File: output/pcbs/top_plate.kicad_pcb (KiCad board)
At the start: 2 copper layers, 93.4 x 87.1 mm, 0 parts

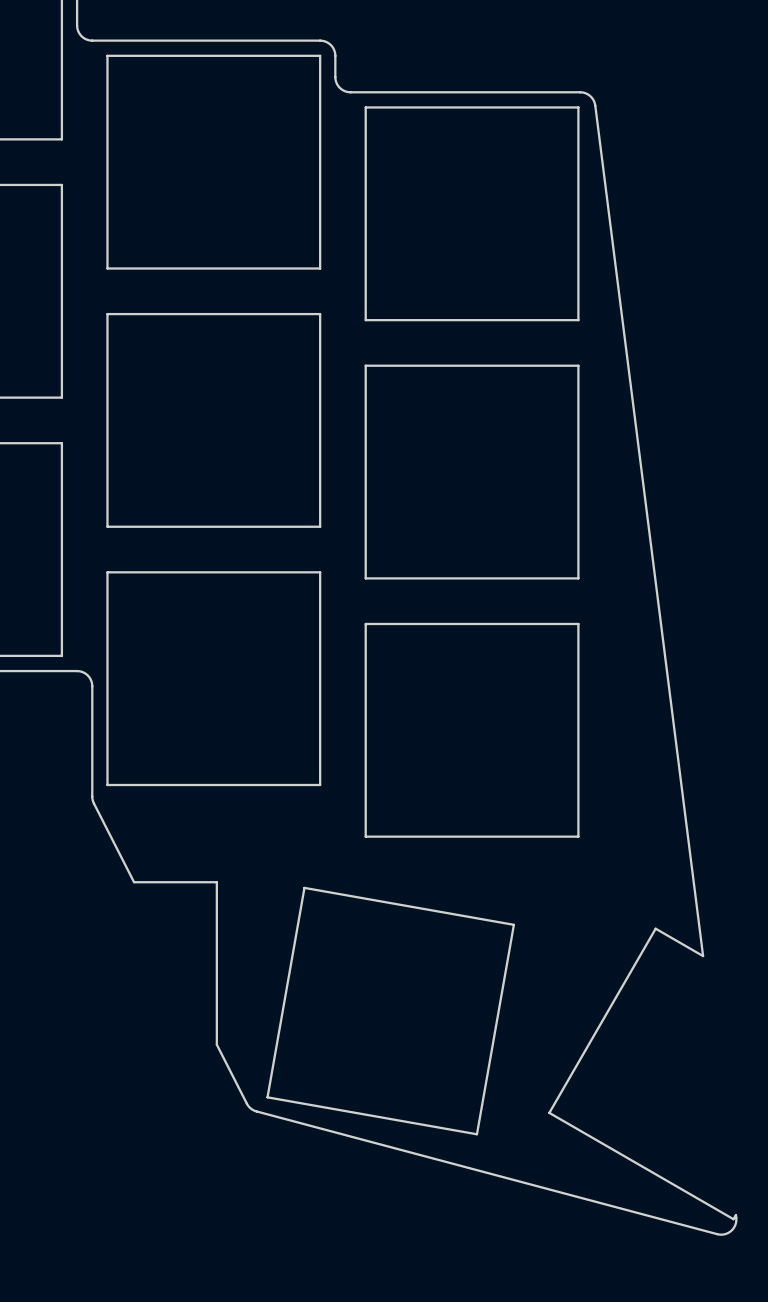
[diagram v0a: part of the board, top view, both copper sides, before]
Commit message: Close the design gaps: coin cell, per-key LEDs, ZMK dongle, JLC files, case
- Reversible footprints (2-pin SMD, SOT-23, slide switch, CR2032 holder,
  M2 holes) that mirror their B-side copper, so one PCB assembles as the
  left half on top and the right half on the bottom.
- Coin cell power path (CR2032 -> switch -> B5819W -> XIAO BAT+), per-key
  0603 LEDs with one PWM-dimmed low-side MOSFET.
- Routed board via Freerouting plus a finisher for nets it misreads, GND
  pours, DRC with no unconnected items, gerbers, BOM and CPL for both sides.
- ZMK v0.3 config: dongle central, two peripheral halves, backlight off by
  default at 10% with idle auto-off; GitHub Actions build.
- OpenSCAD uniboard case generated from the board outline.
- Old hand-routed LiPo board moved to archive/v1-lipo.

Co-Authored-By: Claude Opus 5.5 (1M context) <noreply@anthropic.com>
Claude-Session: https://claude.ai/code/session_01FPyenVXHBDq22rK9XranC3
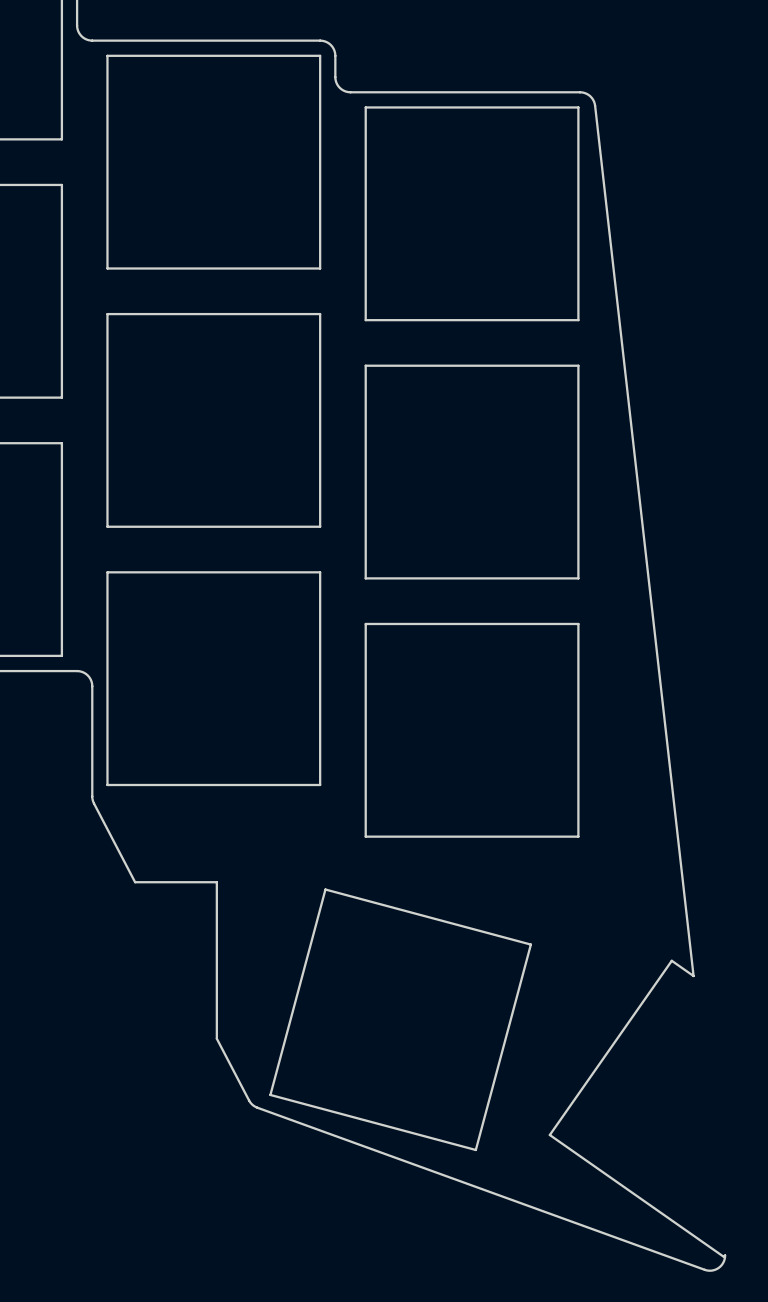
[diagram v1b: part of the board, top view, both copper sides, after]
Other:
- board size 93.4 x 87.1 mm -> 92.7 x 89.5 mm
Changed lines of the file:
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@@
   (page A3)
   (title_block
-    (title "top_plate")
-    (rev "v1.0.0")
-    (company "Unknown")
+    (title top_plate)
+    (rev v1.0.0)
+    (company Unknown)
   )
   (general
@@
       (outputdirectory ""))
   )
-  (net 0 "")
+            (net 0 "")
   (net_class Default "This is the default net class."
     (clearance 0.2)
@@
     (add_net "")
   )
-  (gr_line (start -8 7) (end -8 -41) (angle 90) (layer Edge.Cuts) (width 0.15))
+            (gr_line (start -8 7) (end -8 -41) (angle 90) (layer Edge.Cuts) (width 0.15))
 (gr_line (start -7 -42) (end 8 -42) (angle 90) (layer Edge.Cuts) (width 0.15))
 (gr_line (start 9 -43) (end 9 -54.6) (angle 90) (layer Edge.Cuts) (width 0.15))
@@
 (gr_line (start 43 -53.9) (end 58 -53.9) (angle 90) (layer Edge.Cuts) (width 0.15))
 (gr_line (start 59 -52.9) (end 59 -51.5) (angle 90) (layer Edge.Cuts) (width 0.15))
-(gr_line (start 60 -50.5) (end 75.11877832803583 -50.5) (angle 90) (layer Edge.Cuts) (width 0.15))
-(gr_line (start 76.11083692803584 -49.62577650000003) (end 83.2091607869865 6.362075546015262) (angle 90) (layer Edge.Cuts) (width 0.15))
-(gr_line (start 85.37063644510643 23.41066078283643) (end 85.39157132574321 23.575784130683587) (angle 90) (layer Edge.Cuts) (width 0.15))
-(gr_line (start 84.14207952574318 24.667856730683518) (end 53.808555992537784 16.586633122420103) (angle 90) (layer Edge.Cuts) (width 0.15))
-(gr_line (start 53.17493859253778 16.07424092242009) (end 51.2 12.197274108756417) (angle 90) (layer Edge.Cuts) (width 0.15))
-(gr_line (start 45.750776292981996 1.5) (end 43.1089494 -3.6861233712457846) (angle 90) (layer Edge.Cuts) (width 0.15))
-(gr_line (start 43 -4.140027271245785) (end 43 -11.399999999999999) (angle 90) (layer Edge.Cuts) (width 0.15))
+(gr_line (start 60 -50.5) (end 75.10676247796003 -50.5) (angle 90) (layer Edge.Cuts) (width 0.15))
+(gr_line (start 76.10042267796003 -49.61242549999997) (end 82.58220076816252 7.676038265248053) (angle 90) (layer Edge.Cuts) (width 0.15))
+(gr_line (start 83.31672830212476 27.014027452483596) (end 53.86711680697825 16.343062284377336) (angle 90) (layer Edge.Cuts) (width 0.15))
+(gr_line (start 53.32136560697827 15.865756084377338) (end 51.2 11.80327087166765) (angle 90) (layer Edge.Cuts) (width 0.15))
+(gr_line (start 45.81979470149059 1.5) (end 43.113577 -3.6824962931961807) (angle 90) (layer Edge.Cuts) (width 0.15))
+(gr_line (start 43 -4.145372393196169) (end 43 -11.399999999999999) (angle 90) (layer Edge.Cuts) (width 0.15))
 (gr_line (start 42 -12.399999999999999) (end 26 -12.399999999999999) (angle 90) (layer Edge.Cuts) (width 0.15))
 (gr_line (start 25 -11.399999999999999) (end 25 -6.6) (angle 90) (layer Edge.Cuts) (width 0.15))
@@
 (gr_arc (start 58 -52.9) (end 59 -52.9) (angle -90) (layer Edge.Cuts) (width 0.15))
 (gr_arc (start 60 -51.5) (end 59 -51.5) (angle -90) (layer Edge.Cuts) (width 0.15))
-(gr_arc (start 75.11877832803583 -49.5) (end 76.11083692803584 -49.6257765) (angle -82.77440010116284) (layer Edge.Cuts) (width 0.15))
-(gr_arc (start 84.39951272574318 23.701560630683502) (end 84.14207952574318 24.667856730683503) (angle -112.14341151228206) (layer Edge.Cuts) (width 0.15))
-(gr_arc (start 54.065989192537785 15.6203370224201) (end 53.174938592537785 16.0742409224201) (angle -48.08775587110787) (layer Edge.Cuts) (width 0.15))
-(gr_arc (start 44 -4.140027271245785) (end 43 -4.140027271245785) (angle -26.99443251544085) (layer Edge.Cuts) (width 0.15))
+(gr_arc (start 75.10676247796003 -49.5) (end 76.10042267796003 -49.6124255) (angle -83.5448462900765) (layer Edge.Cuts) (width 0.15))
+(gr_arc (start 83.65740010212473 26.073845152483727) (end 83.31672830212473 27.014027452483727) (angle -110.16568820898408) (layer Edge.Cuts) (width 0.15))
+(gr_arc (start 54.20778860697826 15.402879984377343) (end 53.32136560697826 15.865756084377344) (angle -42.50933832035312) (layer Edge.Cuts) (width 0.15))
+(gr_arc (start 44 -4.145372393196169) (end 43 -4.145372393196169) (angle -27.57285298512062) (layer Edge.Cuts) (width 0.15))
 (gr_arc (start 42 -11.399999999999999) (end 43 -11.399999999999999) (angle -90) (layer Edge.Cuts) (width 0.15))
 (gr_arc (start 26 -11.399999999999999) (end 26 -12.399999999999999) (angle -90) (layer Edge.Cuts) (width 0.15))
@@
 (gr_line (start 75 -49.5) (end 61 -49.5) (angle 90) (layer Edge.Cuts) (width 0.15))
 (gr_line (start 61 -49.5) (end 61 -35.5) (angle 90) (layer Edge.Cuts) (width 0.15))
-(gr_line (start 51.2 12.197274108756417) (end 51.2 1.5) (angle 90) (layer Edge.Cuts) (width 0.15))
-(gr_line (start 51.2 1.5) (end 45.750776292981996 1.5) (angle 90) (layer Edge.Cuts) (width 0.15))
-(gr_line (start 54.5359022 15.660620600000001) (end 68.3232107 18.091695100000003) (angle 90) (layer Edge.Cuts) (width 0.15))
-(gr_line (start 68.3232107 18.091695100000003) (end 70.7542852 4.304386600000001) (angle 90) (layer Edge.Cuts) (width 0.15))
-(gr_line (start 70.7542852 4.304386600000001) (end 56.966976700000004 1.8733121000000015) (angle 90) (layer Edge.Cuts) (width 0.15))
-(gr_line (start 56.966976700000004 1.8733121000000015) (end 54.5359022 15.660620600000001) (angle 90) (layer Edge.Cuts) (width 0.15))
-(gr_line (start 73.0881659 16.684523900000002) (end 85.21252150000001 23.684523900000002) (angle 90) (layer Edge.Cuts) (width 0.15))
-(gr_line (start 85.21252150000001 23.684523900000002) (end 85.37063644510643 23.410660782836487) (angle 90) (layer Edge.Cuts) (width 0.15))
-(gr_line (start 83.2091607869865 6.362075546015241) (end 80.0881659 4.560168300000001) (angle 90) (layer Edge.Cuts) (width 0.15))
-(gr_line (start 80.0881659 4.560168300000001) (end 73.0881659 16.684523900000002) (angle 90) (layer Edge.Cuts) (width 0.15))
+(gr_line (start 51.2 11.80327087166765) (end 51.2 1.5) (angle 90) (layer Edge.Cuts) (width 0.15))
+(gr_line (start 51.2 1.5) (end 45.81979470149059 1.5) (angle 90) (layer Edge.Cuts) (width 0.15))
+(gr_line (start 54.7261566 15.5034436) (end 68.2491182 19.126910199999998) (angle 90) (layer Edge.Cuts) (width 0.15))
+(gr_line (start 68.2491182 19.126910199999998) (end 71.8725848 5.603948599999999) (angle 90) (layer Edge.Cuts) (width 0.15))
+(gr_line (start 71.8725848 5.603948599999999) (end 58.3496232 1.9804820000000003) (angle 90) (layer Edge.Cuts) (width 0.15))
+(gr_line (start 58.3496232 1.9804820000000003) (end 54.7261566 15.5034436) (angle 90) (layer Edge.Cuts) (width 0.15))
+(gr_line (start 73.1185843 18.140387) (end 84.586713 26.1704571) (angle 90) (layer Edge.Cuts) (width 0.15))
+(gr_line (start 84.586713 26.1704571) (end 84.65739070212473 26.06951885248373) (angle 90) (layer Edge.Cuts) (width 0.15))
+(gr_line (start 82.58220076816252 7.676038265247989) (end 81.1486544 6.672258300000003) (angle 90) (layer Edge.Cuts) (width 0.15))
+(gr_line (start 81.1486544 6.672258300000003) (end 73.1185843 18.140387) (angle 90) (layer Edge.Cuts) (width 0.15))
 )

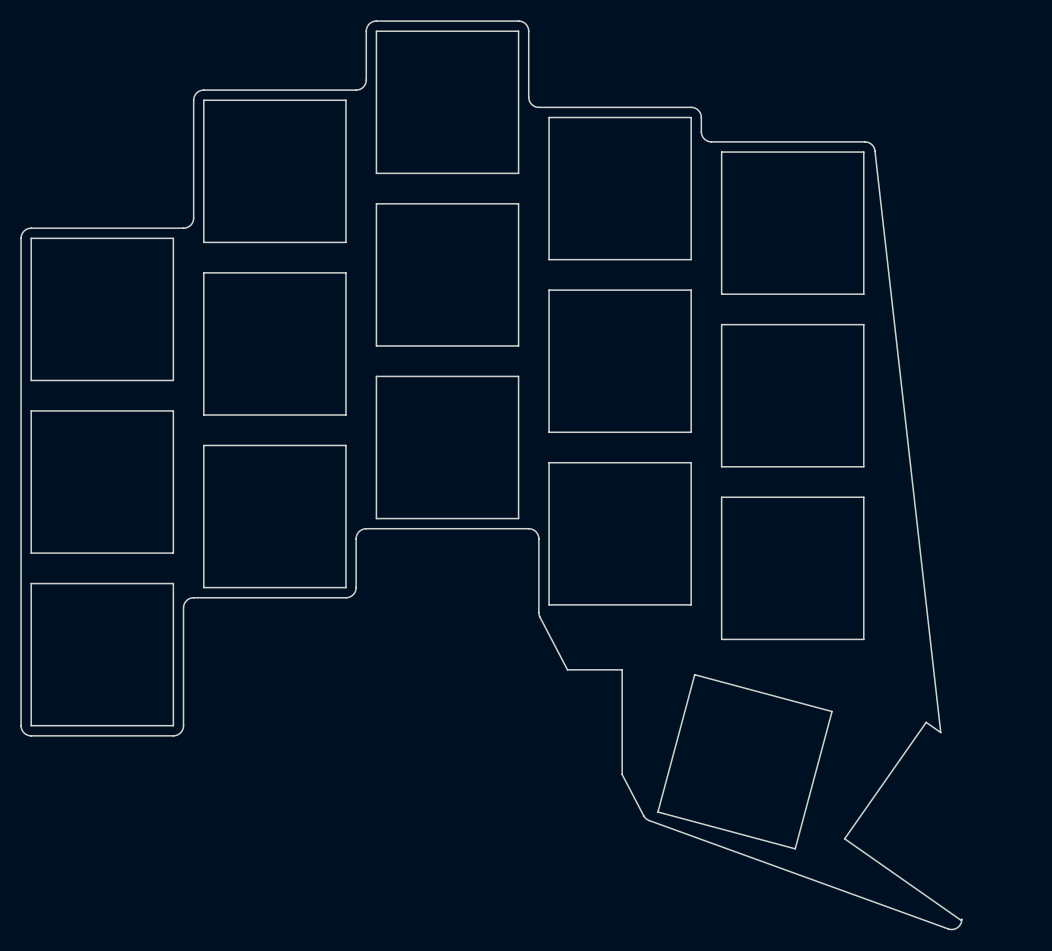
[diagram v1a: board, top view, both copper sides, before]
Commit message: Match the Chocofi key spacing, stagger and thumb cluster
Key centres now come straight from the Chocofi PCB (pashutk/chocofi):
18 x 17 mm pitch, column stagger 12 / 6 / -6.625 / -2.375 mm, thumbs at
fixed offsets from the bottom pinky key with a 0 / -15 / -30 degree fan.

The board top edge and power switch are now set from the pinky key so the
XIAO's top pin row stays on the board, and the thumb M2 hole moved off the
middle thumb diode. finish_routes.py reroutes tracks Freerouting leaves
inside the 0.3 mm edge rule, and the pour ties the XIAO's via-like GND
pads in solidly. Board rerouted, DRC has no new errors, gerbers, CPL and
case regenerated.

Co-Authored-By: Claude Opus 5.5 (1M context) <noreply@anthropic.com>
Claude-Session: https://claude.ai/code/session_01EJCFFVGKLmNFccuN3tJpCU
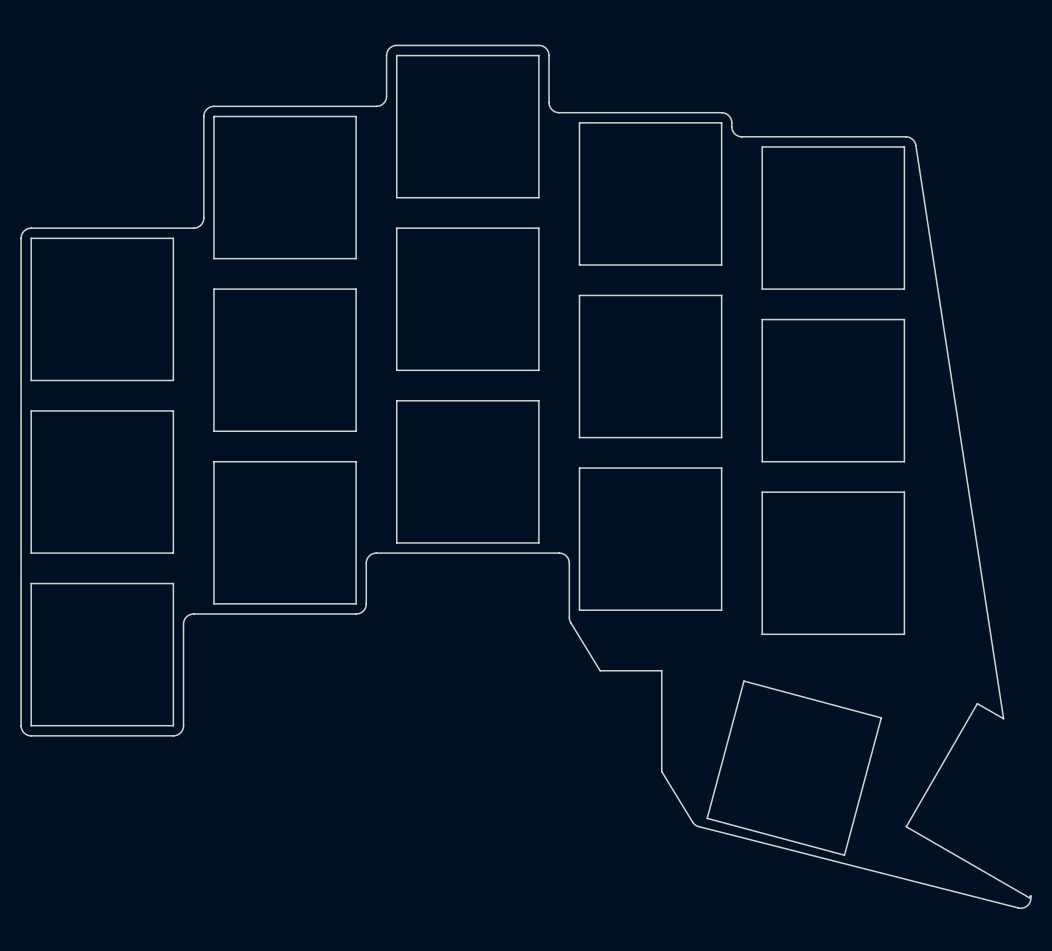
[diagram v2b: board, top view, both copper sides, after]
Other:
- board size 92.7 x 89.5 mm -> 99.5 x 85 mm
